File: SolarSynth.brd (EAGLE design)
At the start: 9 parts, among them IC1 74HCT14N

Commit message: Cap changes
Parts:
- R2: value (none) -> 1k
- U$1: value 080-EU -> 2.2u
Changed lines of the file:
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@@
 <element name="BAT1" library="SparkFun-Electromechanical" package="BATTCON_9V" value="" x="41.91" y="-34.29"/>
 <element name="R1" library="TomW" package="EVUF" value="STARVE" x="-19.05" y="-46.99"/>
-<element name="R2" library="TomW" package="0207/7" value="" x="-20.32" y="-58.42"/>
-<element name="U$1" library="gm-caps-electro-pol" package="080_025" value="080-EU" x="-20.32" y="-64.77"/>
+<element name="R2" library="TomW" package="0207/7" value="1k" x="-20.32" y="-58.42"/>
+<element name="U$1" library="gm-caps-electro-pol" package="080_025" value="2.2u" x="-20.32" y="-64.77"/>
 <element name="R3" library="TomW" package="0207/7" value="" x="-20.32" y="-71.12"/>
 <element name="R4" library="TomW" package="0207/7" value="" x="-20.32" y="-74.93"/>

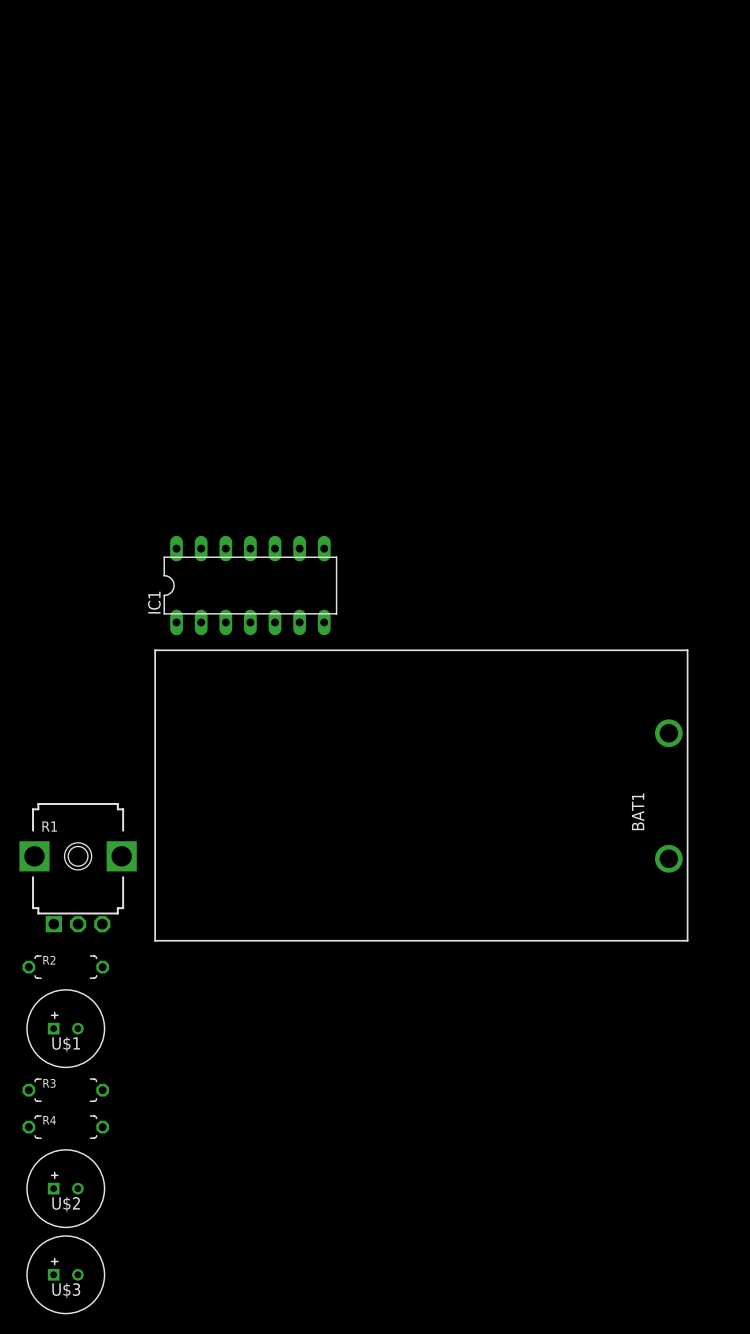
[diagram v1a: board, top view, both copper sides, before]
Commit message: Proto gerbers to OSH park
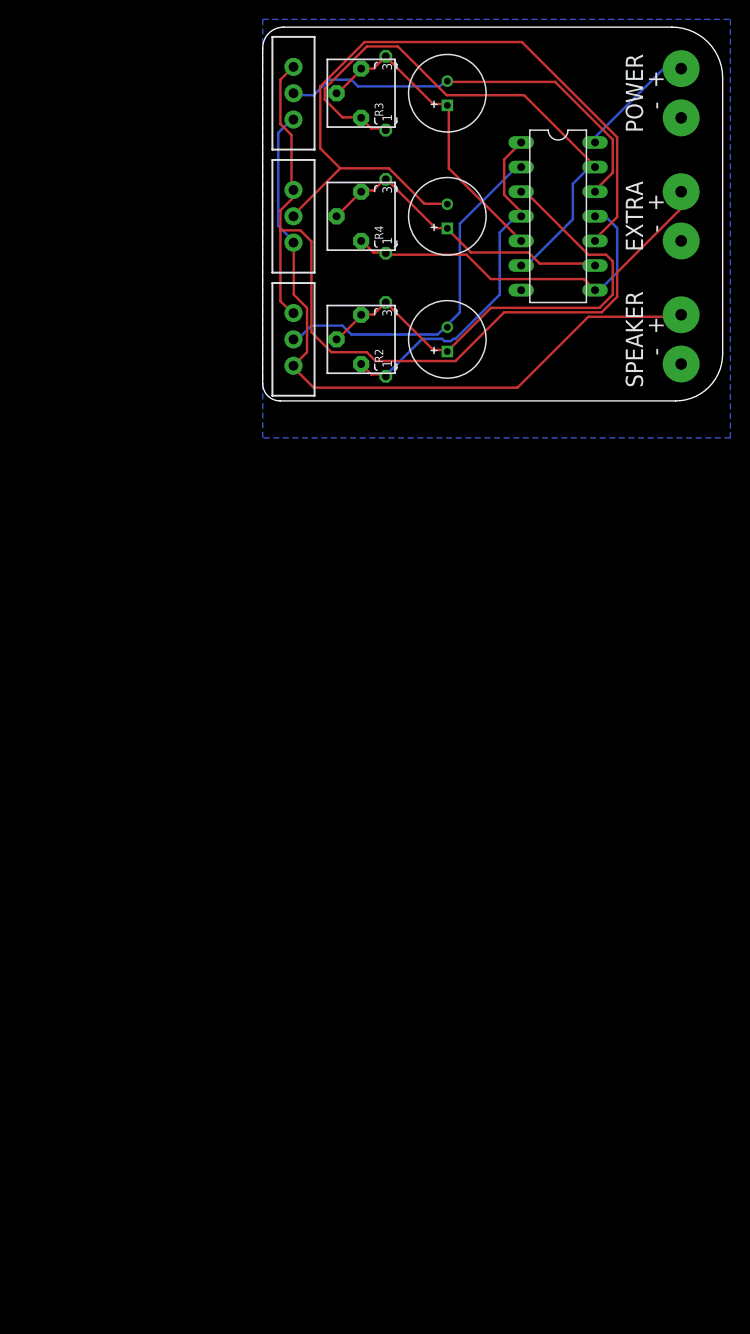
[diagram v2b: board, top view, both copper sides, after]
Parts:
- removed BAT1: (no value), SparkFun-Electromechanical:BATTCON_9V
- removed R1: STARVE, TomW:EVUF
- added S1, S2, S3: (no value), SparkFun-Electromechanical:SWITCH-SPDT_KIT
- added U$4: (no value), TW_logos:MTM_1CM_KEEPOUT
- added VR1, VR2, VR3: (no value), MusicThingModular:BOURNS_3362P_TRIMMER
- R2: value 1k -> (none)
- U$1: value 2.2u -> (none)
- U$2, U$3: value 080-EU -> (none)
- moved U$2 119.7 mm to (19.1, 31.8), turned to 90 degrees
- moved U$3 116.1 mm to (19.1, 19.1), turned to 90 degrees
- moved R3 108.0 mm to (12.7, 31.8), turned to 90 degrees
- moved R4 99.6 mm to (12.7, 19.1), turned to 90 degrees
- moved U$1 81.3 mm to (19.1, 6.35), turned to 90 degrees
- moved R2 72.7 mm to (12.7, 6.35), turned to 90 degrees
- moved IC1 49.6 mm to (30.5, 19.1), turned to 270 degrees
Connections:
- removed net N$1: BAT1.+, IC1.7, R1.1
- removed net N$2: BAT1.-, R1.3
- removed net N$3: IC1.14, R1.2
- new net GND: IC1.7
- new net OUT: S1.1, S2.1, S3.1
- new net OUT2: S1.3, S2.3, S3.3
- new net V+: IC1.14
- net N$10: now also R4.2, VR3.2, VR3.3; no longer R4.1
- net N$11: now also R4.1, VR3.1; no longer R4.2
- net N$12: now also S3.2
- net N$4: now also R2.1, VR1.1; no longer R2.2
- net N$5: now also R2.2, VR1.2, VR1.3; no longer R2.1
- net N$6: now also S1.2
- net N$7: now also R3.2, VR2.2, VR2.3; no longer R3.1
- net N$8: now also R3.1, VR2.1; no longer R3.2
- net N$9: now also S2.2
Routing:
- net OUT: track 0.00 -> 90.0 mm, vias 0 -> 1
- net N$12: track 0.00 -> 77.1 mm
- net OUT2: track 0.00 -> 72.1 mm, vias 0 -> 1
- net N$8: track 0.00 -> 57.8 mm
- net N$5: track 0.00 -> 50.5 mm
- net N$9: track 0.00 -> 43.1 mm
- net N$6: track 0.00 -> 37.2 mm
- net N$4: track 0.00 -> 37.0 mm
- net N$11: track 0.00 -> 36.7 mm
- net N$7: track 0.00 -> 32.4 mm
- net N$10: track 0.00 -> 32.1 mm
- net V+: track 0.00 -> 13.8 mm, vias 0 -> 1
- added copper zone on layer 16, net GND
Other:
- board outline added: 47.5 x 38.6 mm
- board text added: "EXTRA - +"
- board text added: "POWER - +"
- board text added: "SPEAKER - +"
